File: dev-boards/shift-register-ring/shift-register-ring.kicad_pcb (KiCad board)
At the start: 2 copper layers, 40 x 40 mm, 76 parts, among them J0 Pin Headers, J2 JST SH, J3 JST SH, U1 74HC595, U2 74HC595, U3 74HC595, U4 74HC595, U5 74HC595, U6 74HC595

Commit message: Update rear silkscreen
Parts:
- added REF**: OSHW-Logo_7.5x8mm_SilkScreen, Symbol:OSHW-Logo_7.5x8mm_SilkScreen, B.Cu at (170.0, 96.0)
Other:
- board text added: "CLEAR"

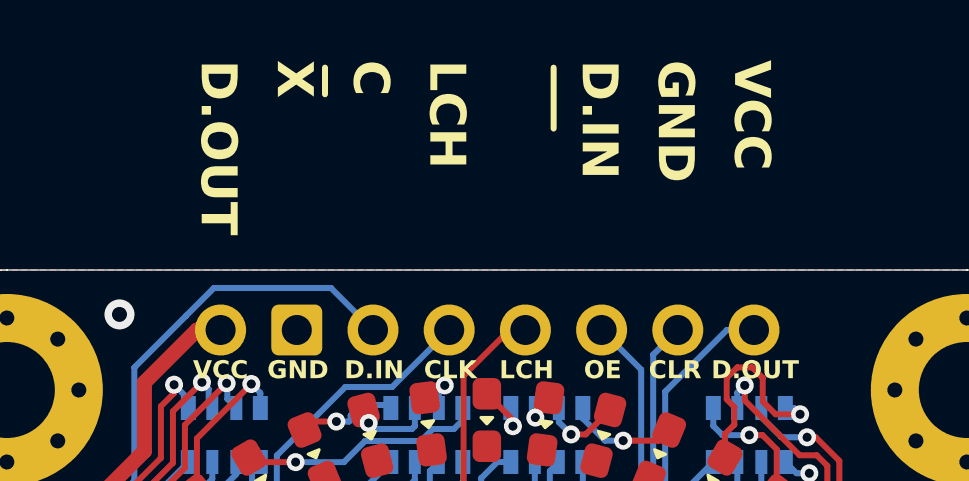
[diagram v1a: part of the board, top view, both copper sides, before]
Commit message: Remove unused off-board silkscreen text
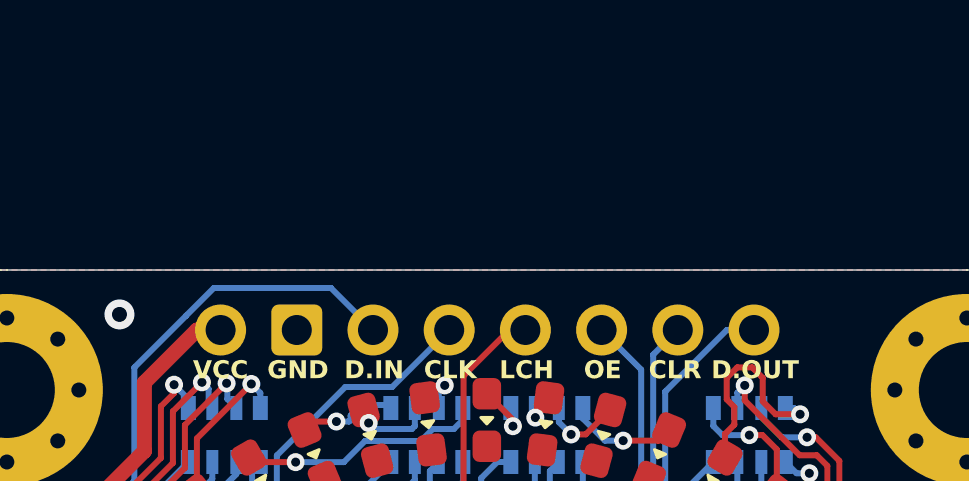
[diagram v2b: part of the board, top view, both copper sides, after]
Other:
- board text removed: "C"
- board text removed: "X"
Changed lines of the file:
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@@
-		(layer "F.SilkS")
-	)
-	(gr_line
-		(start 164.606 68.254)
-		(end 164.606 69.143)
-		(stroke
-			(width 0.2)
-			(type default)
-		)
 		(layer "F.SilkS")
 	)
@@
 		)
 		(fill solid)
-		(layer "F.SilkS")
-	)
-	(gr_line
-		(start 172.226 68.254)
-		(end 172.226 70.286)
-		(stroke
-			(width 0.2)
-			(type default)
-		)
 		(layer "F.SilkS")
 	)
@@
 				(size 0.6 0.6)
 				(thickness 0.12)
-				(bold yes)
-			)
-			(justify right mirror)
-		)
-	)
-	(gr_text "OE"
-		(at 171.21 68 -90)
-		(layer "B.SilkS")
-		(effects
-			(font
-				(size 1.2 1.2)
-				(thickness 0.24)
 				(bold yes)
 			)
@@
 			)
 			(justify top)
-		)
-	)
-	(gr_text "VCC"
-		(at 178.83 68 -90)
-		(layer "F.SilkS")
-		(effects
-			(font
-				(size 1.2 1.2)
-				(thickness 0.24)
-				(bold yes)
-			)
-			(justify left)
-		)
-	)
-	(gr_text "X"
-		(at 163.59 68 -90)
-		(layer "F.SilkS")
-		(effects
-			(font
-				(size 1.2 1.2)
-				(thickness 0.24)
-				(bold yes)
-			)
-			(justify left)
-		)
-	)
-	(gr_text "LCH"
-		(at 168.670002 68 -90)
-		(layer "F.SilkS")
-		(effects
-			(font
-				(size 1.2 1.2)
-				(thickness 0.24)
-				(bold yes)
-			)
-			(justify left)
 		)
 	)
@@
 		)
 	)
-	(gr_text "D.IN"
-		(at 173.75 68 -90)
-		(layer "F.SilkS")
-		(effects
-			(font
-				(size 1.2 1.2)
-				(thickness 0.24)
-				(bold yes)
-			)
-			(justify left)
-		)
-	)
 	(gr_text "LCH"
 		(at 171.323 77.978 0)
@@
 		)
 	)
-	(gr_text "C"
-		(at 166.13 68 -90)
-		(layer "F.SilkS")
-		(effects
-			(font
-				(size 1.2 1.2)
-				(thickness 0.24)
-				(bold yes)
-			)
-			(justify left)
-		)
-	)
 	(gr_text "CLK"
 		(at 168.783 77.978 0)
@@
 		)
 	)
-	(gr_text "GND"
-		(at 176.29 68 -90)
-		(layer "F.SilkS")
-		(effects
-			(font
-				(size 1.2 1.2)
-				(thickness 0.24)
-				(bold yes)
-			)
-			(justify left)
-		)
-	)
 	(gr_text "D.OUT"
 		(at 178.943 77.978 0)
@@
 		)
 	)
-	(gr_text "D.OUT"
-		(at 161.05 68 -90)
-		(layer "F.SilkS")
-		(effects
-			(font
-				(size 1.2 1.2)
-				(thickness 0.24)
-				(bold yes)
-			)
-			(justify left)
-		)
-	)
